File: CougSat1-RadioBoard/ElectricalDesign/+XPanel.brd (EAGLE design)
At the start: 79 x 90 mm, 68 parts, among them J1 ADCS Connector, J2 Low Gain +, J3 Low Gain -, J4 Low Gain Coax, J5 GPS Coax, J6 EPS Connector, U1 AD8515, U2 AD8542, U3 AD7291

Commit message: Fixed Errors
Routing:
- net AVDD: track 78.1 -> 83.5 mm
- net AGND: track 245.3 -> 243.3 mm
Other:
- board text added: "AVDD"
- board text added: "AVREF UNBUF"
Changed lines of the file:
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@@
 <wire x1="-13.656853125" y1="-13.343146875" x2="-4.5" y2="-22.5" width="3.2" layer="51"/>
 <text x="-15.3" y="39.3" size="1.016" layer="25">+X Panel V1.0</text>
+<text x="-19.1" y="32" size="0.5" layer="25">AVDD</text>
+<text x="-18.4" y="34.3" size="0.5" layer="25">AVREF UNBUF</text>
 </plain>
 <attributes>
@@
 </element>
 <element name="H1" library="CougsInSpace-Hardware" package="MOUNTING_HOLE-2.2" value="M2" x="30.3895" y="-25" locked="yes" smashed="yes">
-<attribute name="NAME" x="30.9895" y="-27.9" size="0.8" layer="25" font="vector" ratio="15" align="center"/>
 <attribute name="SKU" value="48-003x" x="73.5695" y="-52.94" size="1.778" layer="27" display="off"/>
 </element>
 <element name="H10" library="CougsInSpace-Hardware" package="MOUNTING_HOLE-3.3" value="M3" x="-14" y="0" locked="yes" smashed="yes">
-<attribute name="NAME" x="-11.4" y="3.6" size="0.8" layer="25" font="vector" ratio="15" align="center"/>
 <attribute name="SKU" value="48-004x" x="26.64" y="-40.64" size="1.778" layer="27" display="off"/>
 </element>
 <element name="H2" library="CougsInSpace-Hardware" package="MOUNTING_HOLE-2.2" value="M2" x="-29.596" y="40" locked="yes" smashed="yes">
-<attribute name="NAME" x="-29.596" y="42.9" size="0.8" layer="25" font="vector" ratio="15" align="center"/>
 <attribute name="SKU" value="48-003x" x="18.664" y="12.06" size="1.778" layer="27" display="off"/>
 </element>
 <element name="H3" library="CougsInSpace-Hardware" package="MOUNTING_HOLE-2.2" value="M2" x="-30.3895" y="-25" locked="yes" smashed="yes">
-<attribute name="NAME" x="-27.5895" y="-26.8" size="0.8" layer="25" font="vector" ratio="15" align="center"/>
 <attribute name="SKU" value="48-003x" x="22.9505" y="-52.94" size="1.778" layer="27" display="off"/>
 </element>
 <element name="H4" library="CougsInSpace-Hardware" package="MOUNTING_HOLE-2.2" value="M2" x="29.596" y="40" locked="yes" smashed="yes">
-<attribute name="NAME" x="28.696" y="37.1" size="0.8" layer="25" font="vector" ratio="15" align="center"/>
 <attribute name="SKU" value="48-003x" x="88.016" y="12.06" size="1.778" layer="27" display="off"/>
 </element>
 <element name="H5" library="CougsInSpace-Hardware" package="MOUNTING_HOLE-3.3" value="M3" x="-36.5" y="-42" locked="yes" smashed="yes">
-<attribute name="NAME" x="-36.5" y="-39.1" size="0.8" layer="25" font="vector" ratio="15" align="center"/>
 <attribute name="SKU" value="48-004x" x="-21.26" y="-82.64" size="1.778" layer="27" display="off"/>
 </element>
 <element name="H6" library="CougsInSpace-Hardware" package="MOUNTING_HOLE-3.3" value="M3" x="-36.5" y="42" locked="yes" smashed="yes">
-<attribute name="NAME" x="-35.2" y="38" size="0.8" layer="25" font="vector" ratio="15" align="center"/>
 <attribute name="SKU" value="48-004x" x="-16.18" y="1.36" size="1.778" layer="27" display="off"/>
 </element>
 <element name="H7" library="CougsInSpace-Hardware" package="MOUNTING_HOLE-3.3" value="M3" x="36.5" y="42" locked="yes" smashed="yes">
-<attribute name="NAME" x="36.6" y="37.9" size="0.8" layer="25" font="vector" ratio="15" align="center"/>
 <attribute name="SKU" value="48-004x" x="61.9" y="1.36" size="1.778" layer="27" display="off"/>
 </element>
 <element name="H8" library="CougsInSpace-Hardware" package="MOUNTING_HOLE-3.3" value="M3" x="36.5" y="-42" locked="yes" smashed="yes">
-<attribute name="NAME" x="37.5" y="-38" size="0.8" layer="25" font="vector" ratio="15" align="center"/>
 <attribute name="SKU" value="48-004x" x="66.98" y="-82.64" size="1.778" layer="27" display="off"/>
 </element>
 <element name="H9" library="CougsInSpace-Hardware" package="MOUNTING_HOLE-3.3" value="M3" x="14" y="0" locked="yes" smashed="yes">
-<attribute name="NAME" x="12.3" y="3.9" size="0.8" layer="25" font="vector" ratio="15" align="center"/>
 <attribute name="SKU" value="48-004x" x="49.56" y="-40.64" size="1.778" layer="27" display="off"/>
 </element>
@@
 <attribute name="SKU" value="26-0008" x="-45.8" y="91.54" size="1.778" layer="27" rot="R180" display="off"/>
 </element>
-<element name="TP2" library="CougsInSpace-Connectors" package="SMD-C-1.25" value="TEST_POINT-SMD-C-1.25" x="-17.7" y="30.8" smashed="yes">
-<attribute name="NAME" x="-17.7" y="32.3" size="0.8" layer="25" font="vector" ratio="15" align="center"/>
-</element>
+<element name="TP2" library="CougsInSpace-Connectors" package="SMD-C-1.25" value="TEST_POINT-SMD-C-1.25" x="-17.7" y="30.8" smashed="yes"/>
 <element name="U1" library="CougsInSpace-IC-Amplifiers" package="SOT23-5" value="AD8515" x="-11.3" y="29.6" smashed="yes">
 <attribute name="NAME" x="-8.2" y="30.2" size="0.8" layer="25" font="vector" ratio="15" align="center"/>
@@
 </element>
 <element name="H11" library="CougsInSpace-Hardware" package="MOUNTING_HOLE-M2_NUT" value="M2 Nut - 1mm" x="3.5" y="-40.5" locked="yes" smashed="yes">
-<attribute name="NAME" x="5.3" y="-37" size="0.8" layer="25" font="vector" ratio="15" align="center"/>
 <attribute name="SKU" value="48-0074" x="3.5" y="-40.5" size="1.778" layer="27" display="off"/>
 </element>
 <element name="H12" library="CougsInSpace-Hardware" package="MOUNTING_HOLE-M2_NUT" value="M2 Nut - 1mm" x="-3.5" y="-40.5" locked="yes" smashed="yes">
-<attribute name="NAME" x="-0.5" y="-37.6" size="0.8" layer="25" font="vector" ratio="15" align="center"/>
 <attribute name="SKU" value="48-0074" x="-3.5" y="-40.5" size="1.778" layer="27" display="off"/>
 </element>
-<element name="TP1" library="CougsInSpace-Connectors" package="SMD-C-1.25" value="TEST_POINT-SMD-C-1.25" x="-15.7" y="33.2" smashed="yes">
-<attribute name="NAME" x="-17.1" y="34.6" size="0.8" layer="25" font="vector" ratio="15" align="center"/>
-</element>
+<element name="TP1" library="CougsInSpace-Connectors" package="SMD-C-1.25" value="TEST_POINT-SMD-C-1.25" x="-15.7" y="33.2" smashed="yes"/>
 <element name="RN3" library="CougsInSpace-Resistors" package="3264" value="10kΩ 5%" x="-8.3" y="20" smashed="yes" rot="R180">
 <attribute name="NAME" x="-13" y="18.2" size="0.8" layer="25" font="vector" ratio="15" rot="R180" align="center"/>
@@
 <wire x1="-6.95" y1="27.45" x2="-6.95" y2="27.55" width="0.2" layer="1"/>
 <wire x1="-6.95" y1="27.55" x2="-3.4" y2="31.1" width="0.2" layer="1"/>
-<wire x1="-10.25" y1="-31.2" x2="-13.9" y2="-31.2" width="0.2" layer="1"/>
+<wire x1="-10.25" y1="-31.2" x2="-11.1" y2="-31.2" width="0.2" layer="1"/>
 <wire x1="29.55" y1="-7.15" x2="29.55" y2="-6" width="0.2" layer="1"/>
 <wire x1="29.9" y1="-8.3" x2="29.9" y2="-7.5" width="0.2" layer="1"/>
@@
 <wire x1="-0.525" y1="19.2" x2="-0.525" y2="20.475" width="0.2" layer="1"/>
 <wire x1="-0.525" y1="20.475" x2="0.5" y2="21.5" width="0.2" layer="1"/>
-<wire x1="0.5" y1="26.2" x2="0.2" y2="26.5" width="0.2" layer="1"/>
-<wire x1="0.5" y1="21.5" x2="0.5" y2="26.2" width="0.2" layer="1"/>
-<wire x1="0.2" y1="26.5" x2="-0.3" y2="26.5" width="0.2" layer="1"/>
 <wire x1="-17.15" y1="5.2" x2="-19.3" y2="5.2" width="0.2" layer="1"/>
 <wire x1="-19.3" y1="5.2" x2="-19.4" y2="5.3" width="0.2" layer="1"/>
@@
 <via x="-14.2" y="14.6" extent="1-16" drill="0.35"/>
 <contactref element="C14" pad="2"/>
-<wire x1="-13.9" y1="-31.2" x2="-16.1" y2="-29" width="0.2" layer="1"/>
-<wire x1="-16.1" y1="-29" x2="-16.1" y2="-14.9" width="0.2" layer="1"/>
+<wire x1="-11.1" y1="-31.2" x2="-16.1" y2="-26.2" width="0.2" layer="1"/>
+<wire x1="-16.1" y1="-26.2" x2="-16.1" y2="-14.9" width="0.2" layer="1"/>
 <wire x1="-16.1" y1="-14.9" x2="-18.3" y2="-12.7" width="0.2" layer="1"/>
 <wire x1="-18.3" y1="-12.7" x2="-20.7" y2="-12.7" width="0.2" layer="1"/>
-<wire x1="-0.1" y1="15.55" x2="-0.1" y2="18.775" width="0.2" layer="1"/>
-<wire x1="-0.1" y1="18.775" x2="-0.525" y2="19.2" width="0.2" layer="1"/>
+<wire x1="-0.1" y1="15.55" x2="-0.1" y2="18.1" width="0.16" layer="1"/>
+<wire x1="-0.525" y1="18.525" x2="-0.525" y2="19.2" width="0.16" layer="1"/>
+<wire x1="-0.1" y1="18.1" x2="-0.525" y2="18.525" width="0.16" layer="1"/>
+<wire x1="0.5" y1="21.5" x2="0.5" y2="25.65" width="0.16" layer="1"/>
+<wire x1="0.5" y1="25.65" x2="-0.3" y2="26.45" width="0.16" layer="1"/>
 </signal>
 <signal name="AVDD">
@@
 <wire x1="-21.2" y1="8.6" x2="-15.7" y2="8.6" width="0.2" layer="1"/>
 <via x="-15.7" y="8.6" extent="1-16" drill="0.35"/>
-<wire x1="-15.7" y1="8.6" x2="-15.7" y2="17.8" width="0.2" layer="16"/>
-<wire x1="-15.7" y1="17.8" x2="-10.2" y2="23.3" width="0.2" layer="16"/>
 <contactref element="C14" pad="1"/>
 <wire x1="-0.1" y1="14.05" x2="-2.95" y2="14.05" width="0.2" layer="1"/>
@@
 <wire x1="-3.5" y1="22.5" x2="-3.9" y2="22.9" width="0.2" layer="1"/>
 <wire x1="-3.5" y1="14.6" x2="-3.5" y2="22.5" width="0.2" layer="1"/>
+<wire x1="-15.7" y1="22.8" x2="-18.3" y2="25.4" width="0.2" layer="16"/>
+<wire x1="-18.3" y1="25.4" x2="-18.3" y2="27" width="0.2" layer="16"/>
+<wire x1="-18.3" y1="27" x2="-16.3" y2="29" width="0.2" layer="16"/>
+<wire x1="-15.7" y1="8.6" x2="-15.7" y2="22.8" width="0.2" layer="16"/>
 </signal>
 <signal name="DGND">

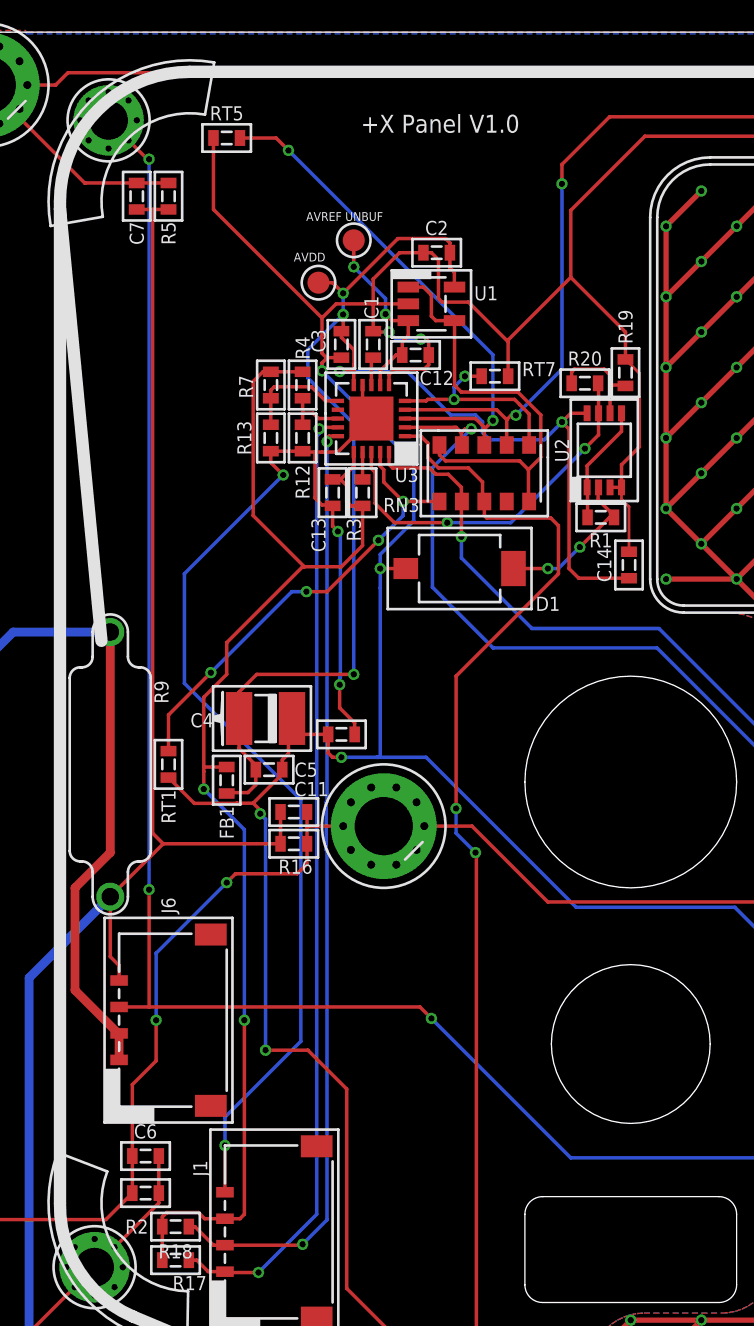
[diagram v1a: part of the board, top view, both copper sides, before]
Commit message: Fixed Spacing
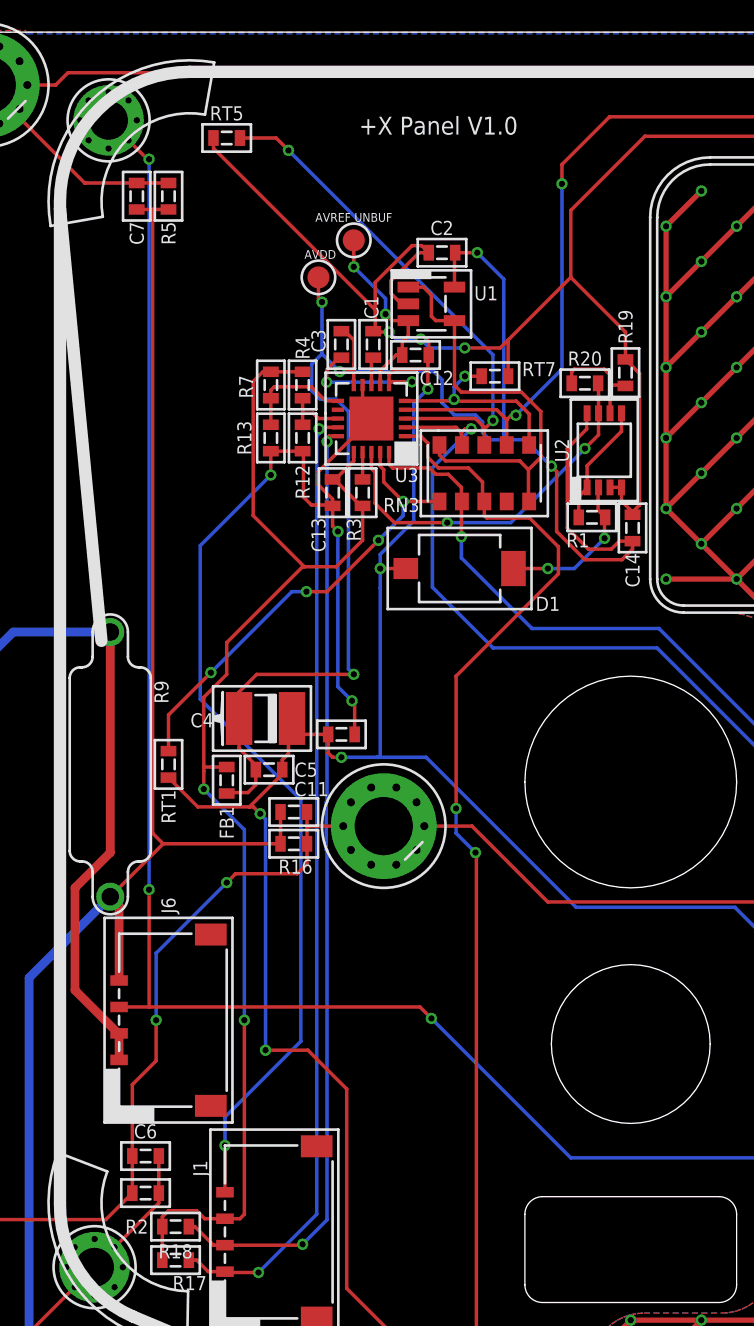
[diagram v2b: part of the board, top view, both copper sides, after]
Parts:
- moved C14 2.11 mm to (0.10, 16.9)
- moved R1 0.50 mm to (-2.20, 17.5)
- moved C2 0.30 mm to (-10.7, 32.5)
- moved TP2 0.30 mm to (-17.7, 31.1)
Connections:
- net IN-1 renamed PHOTODIODE_IN-1
- net IN-2 renamed PHOTODIODE_IN-2
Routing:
- net AVDD: track 83.5 -> 95.4 mm
- net DGND: track 75.0 -> 76.2 mm
- net THERM-2: track 63.4 -> 62.7 mm
- net AGND: track 243.3 -> 243.5 mm, vias 9 -> 12

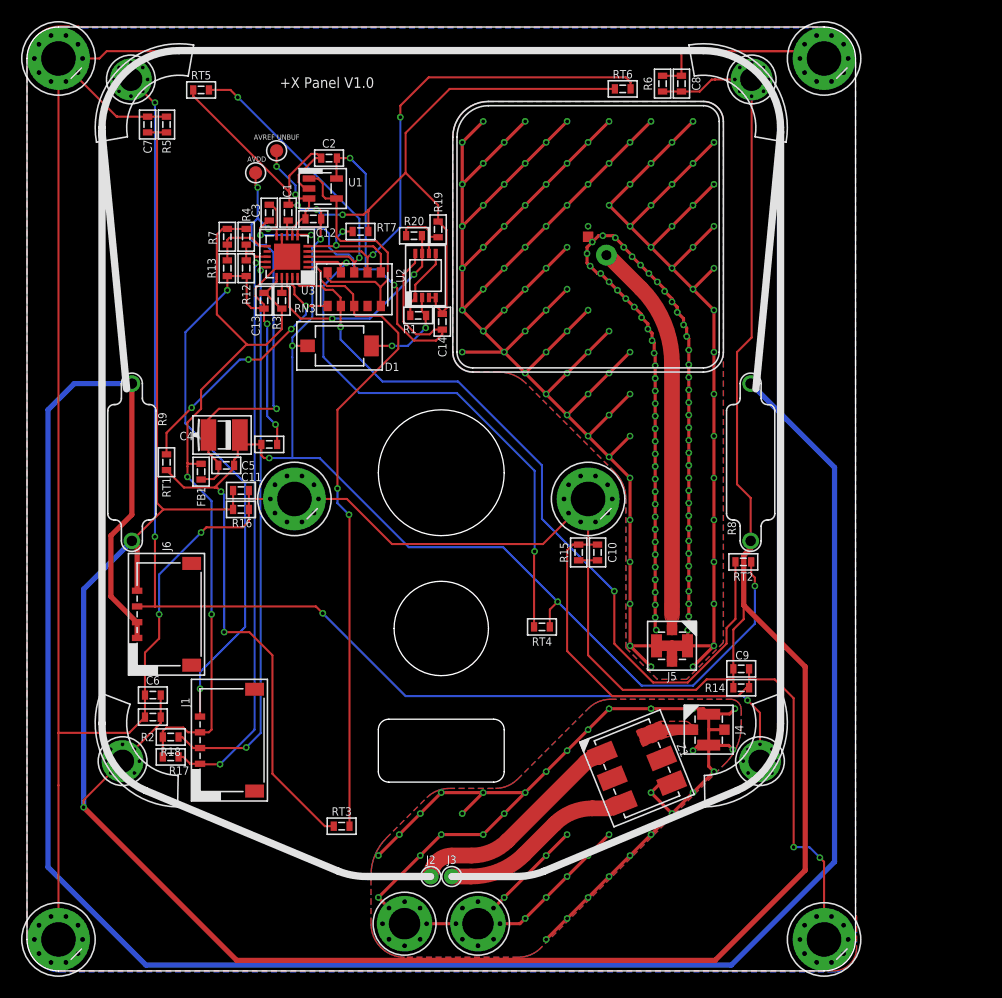
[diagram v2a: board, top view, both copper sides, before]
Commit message: Added Variant Label
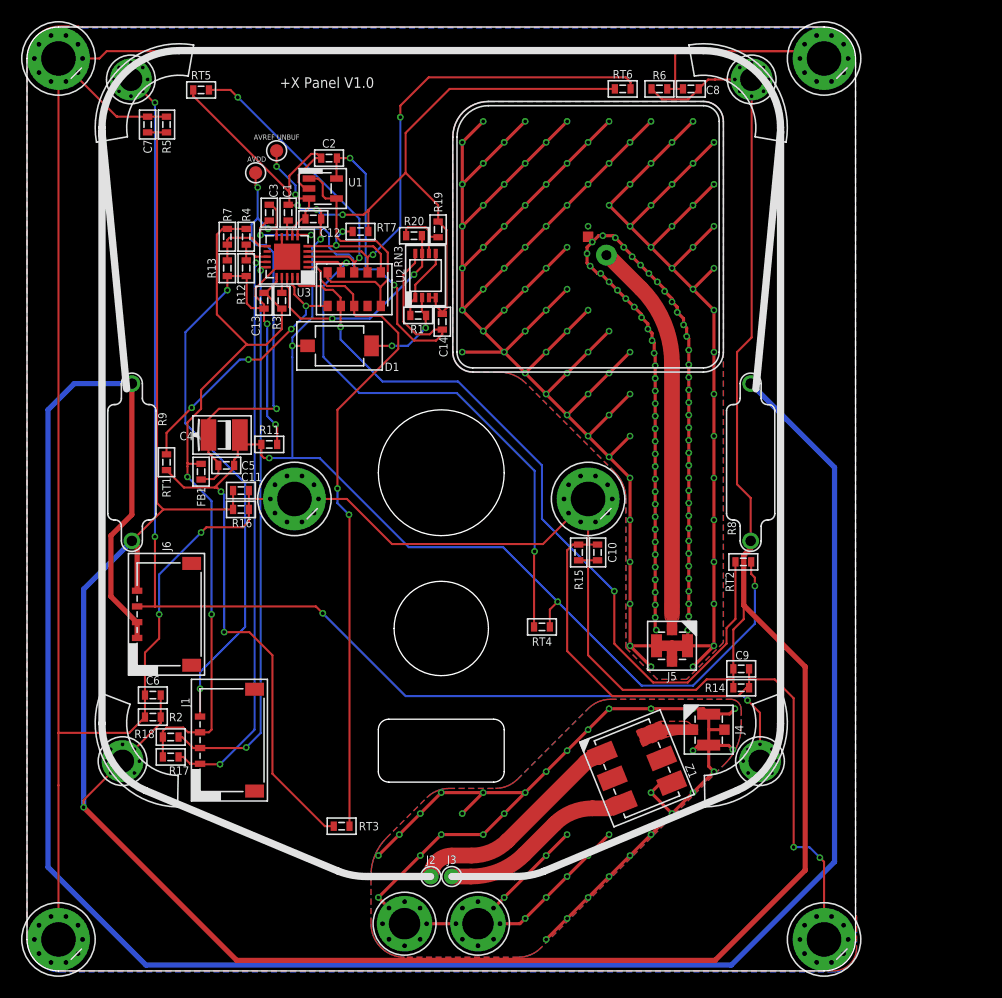
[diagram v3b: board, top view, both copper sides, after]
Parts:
- moved C8 1.03 mm to (23.8, 39.1), turned to 0 degrees
- moved R6 0.58 mm to (20.8, 39.1), turned to 0 degrees
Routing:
- net PGND: track 324.5 -> 326.3 mm
- net CHASSIS: track 471.5 -> 472.4 mm

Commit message: Exported Schematic
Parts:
- removed C14: 100nF 10%, CougsInSpace-Capacitors:1608
- removed R19: 1kΩ 0.1%, CougsInSpace-Resistors:1608
- removed R20: 33kΩ 1%, CougsInSpace-Resistors:1608
- removed U2: AD8542, CougsInSpace-IC-Amplifiers:MSOP-8
- R1: value 10Ω 5% -> 2kΩ 0.1%
- moved R1 2.90 mm to (-4.20, 15.4), turned to 270 degrees
- moved D1 0.30 mm to (-9.40, 14.6), turned to 180 degrees
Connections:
- removed net OUT1_IN+2: R1.2, U2.1, U2.5
- removed net PHOTODIODE_IN-1: D1.C, R1.1, U2.2
- removed net PHOTODIODE_IN-2: R19.2, R20.1, U2.6
- net 3.3V: now also D1.C
- net AGND: now also R1.1; no longer C14.2, D1.A, R19.1, U2.3, U2.4
- net AVDD: no longer C14.1, U2.8
- net PHOTO: now also D1.A, R1.2; no longer R20.2, U2.7
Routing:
- net AVDD: track 95.4 -> 60.1 mm
- net CHASSIS: track 472.4 -> 457.7 mm
- net PHOTODIODE_IN-1: track 9.30 -> 0.00 mm, vias 2 -> 0
- net AGND: track 243.5 -> 234.2 mm
- net OUT1_IN+2: track 6.93 -> 0.00 mm
- net PHOTODIODE_IN-2: track 6.09 -> 0.00 mm
- net THERM-2: track 62.7 -> 57.8 mm
- net 3.3V: track 73.9 -> 78.6 mm
- net PHOTO: track 21.1 -> 16.9 mm
- net PGND: track 326.3 -> 324.6 mm
- net THERM-1: track 75.3 -> 76.1 mm
